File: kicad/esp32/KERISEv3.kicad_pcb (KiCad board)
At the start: 2 copper layers, 49 x 49 mm, 114 parts, among them P1 Motor_L, P10 PR_Host, P11 PR_Slave, P12 ENC_Host, P13 ENC_Slave, P14 ENC_Host, P15 ENC_Slave, P16 UART, P17 Fan, P18 PCB_ANT, P19 ANT_Host, P2 Motor_R, P3 Battery, P4 PR_Host, P5 PR_Slave, P6 PR_Host, P7 PR_Slave, P8 PR_Host, P9 PR_Slave, Q1 IRFML8244, Q2 IRFML8244, Q3 IRFML8244, Q4 IRFML8244, Q5 BSS138, Q6 IRFML8244, SW1 RESET, SW2 SW_PUSH_SMALL, U1 ESP32, U10 MPU6500, U11 AS5145, U12 AS5145, U2 XTAL, U3 FLASH, U4 DRV8835, U5 NJM2884, U6 AD8601, U7 AD8601, U8 AD8601, U9 AD8601

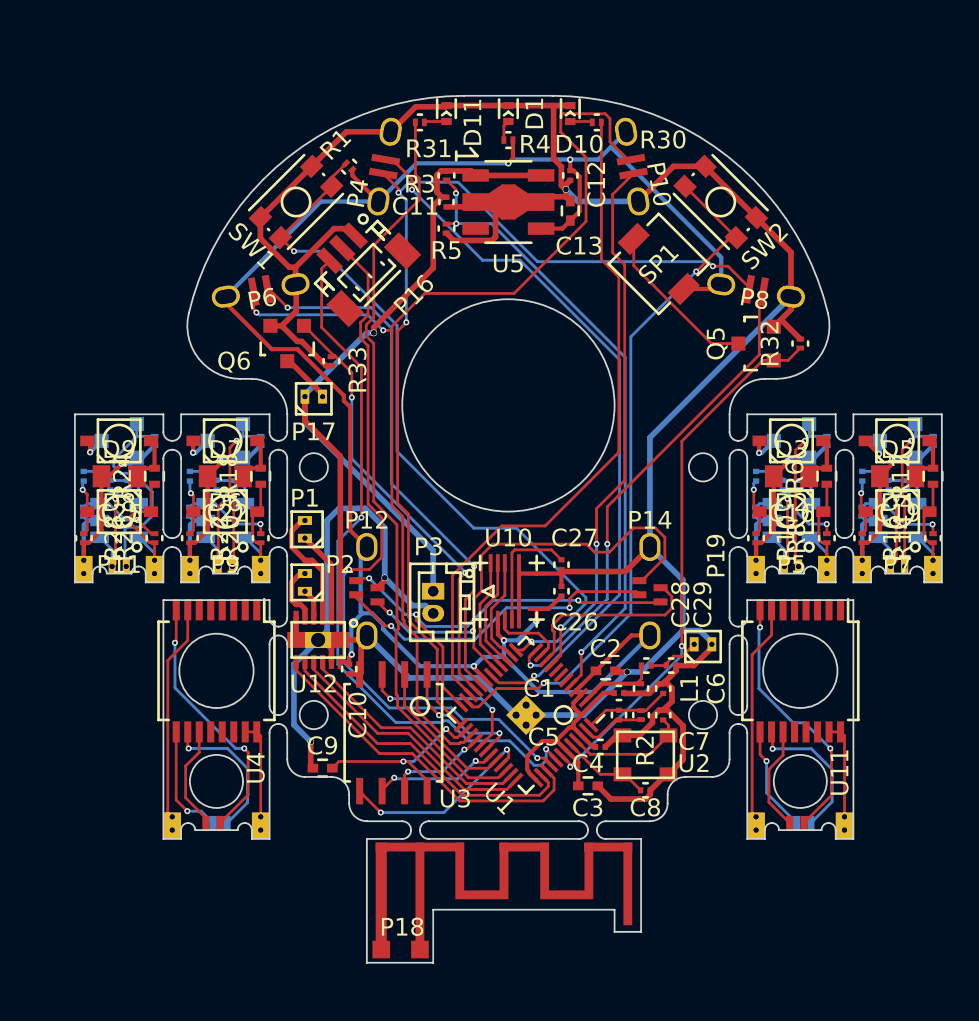
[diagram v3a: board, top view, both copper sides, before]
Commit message: 2輪の基板を作成
部品を配置
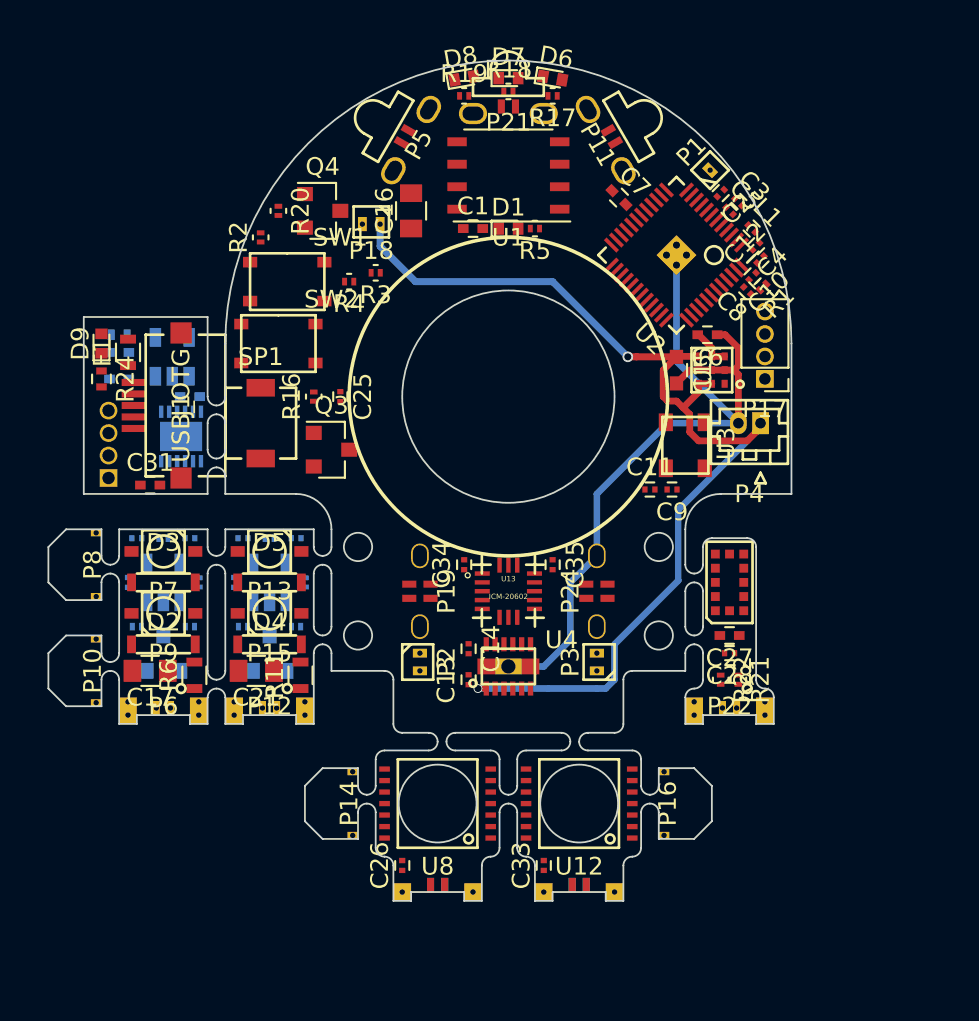
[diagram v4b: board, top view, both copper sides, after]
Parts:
- removed the C11 at (145.0, 91.0)
- removed the C12 at (152.0, 89.5)
- removed the C17 at (170.0, 107.0)
- removed the C18 at (168.5, 106.5)
- removed the C19 at (170.5, 106.5)
- removed the C21 at (130.5, 106.5)
- removed the C22 at (132.5, 106.5)
- removed the D4 at (170.5, 108.5)
- removed the D5 at (170.5, 104.5)
- removed the D6 at (132.5, 108.5)
- removed the D7 at (132.5, 104.5)
- removed the P12 at (140.5, 113.0)
- removed the P18 at (141.0, 132.8)
- removed the P6 at (134.5, 96.0)
- removed the Q2 at (170.5, 104.5)
- removed Q5: BSS138, TO_SOT_Packages_SMD:SOT-23
- removed the R12 at (172.5, 106.5)
- removed the R13 at (171.0, 107.0)
- removed the R14 at (172.5, 110.0)
- removed the R15 at (168.5, 108.5)
- removed the R17 at (172.5, 104.5)
- removed the R18 at (134.5, 106.5)
- removed the R20 at (134.5, 110.0)
- removed R29, R32: 10k, Resistors_SMD:R_0201
- removed the U3 at (142.0, 121.0)
- removed the U7 at (170.5, 109.0)
- added C15: 10u, Capacitors_SMD:C_0603, F.Cu at (158.0, 100.5)
- added C16: 47u, Capacitors_SMD:C_0805, F.Cu at (143.0, 91.5)
- added C2: 2.4p, Capacitors_SMD:C_0201, F.Cu at (160.5, 90.5)
- added C24: 0.1u, Capacitors_SMD:C_0201, B.Cu at (136.5, 110.0)
- added C25: 0.1u, Capacitors_SMD:C_0201, F.Cu at (139.0, 102.0)
- added C3: 3.9p, Capacitors_SMD:C_0201, F.Cu at (161.5, 91.0)
- added C30: 4.7u, Capacitors_SMD:C_0402, B.Cu at (126.5, 99.5)
- added C31: 0.1u, Capacitors_SMD:C_0402, F.Cu at (128.2, 107.0)
- added C32: 4.7u, Capacitors_SMD:C_0402, B.Cu at (126.5, 101.0)
- added C33: 0.1u, Capacitors_SMD:C_0201, F.Cu at (150.5, 128.5)
- added C34: 0.1u, Capacitors_SMD:C_0201, F.Cu at (146.0, 111.5)
- added C35: 0.1u, Capacitors_SMD:C_0201, F.Cu at (151.0, 111.5)
- added C4: 0.1u, Capacitors_SMD:C_0201, F.Cu at (162.5, 93.5)
- added D8: LED, LEDs:LED_0402, F.Cu at (146.0, 84.0)
- added D9: Status, LEDs:LED_0402, F.Cu at (125.5, 99.0)
- added F1: FEMTOSMDC035F-02, Resistors_SMD:R_0603, F.Cu at (127.0, 99.5)
- added J1: USB_OTG, mouse:ZX62R-B-5P, F.Cu at (130.0, 102.5)
- added P1: ANT, mouse:SMD_conn_1, F.Cu at (159.9, 89.2)
- added P10: Partition, mouse:Partition_Slave, F.Cu at (125.5, 117.5)
- added P17: COM, Pin_Headers:Pin_Header_Straight_1x04_Pitch1.27mm, F.Cu at (163.0, 101.0)
- added P20: ENC_Slave, mouse:STAND_AS_SLAVE, B.Cu at (144.5, 130.0)
- added P21: ToF_Host, mouse:STAND_PR_HOST, F.Cu at (148.5, 86.0)
- added P22: ToF_Slave, mouse:STAND_PR_SLAVE, F.Cu at (161.0, 120.0)
- added P23: COM, Socket_Strips:Socket_Strip_Straight_1x04_Pitch1.27mm, B.Cu at (125.9, 106.6)
- added P24: ENC_Host, mouse:STAND_AS_HOST, F.Cu at (153.5, 113.0)
- added P25: ENC_Slave, mouse:STAND_AS_SLAVE, B.Cu at (152.5, 130.0)
- added U1: FLASH, mouse:DFN-8-1EP_6x5mm_Pitch1.27mm_SmallFlag, F.Cu at (148.5, 89.5)
- added U13: ICM-20602, mouse:LGA-16-3x3, F.Cu at (148.5, 113.0)
- added U9: VL53L0X, mouse:VL53L0X, F.Cu at (161.0, 112.5)
- C13: value 4.7u -> 0.1u; footprint Capacitors_SMD:C_0402 -> Capacitors_SMD:C_0201
- C20: value 22p -> 0.1u
- C27: value 0.1u -> 4.7u; footprint Capacitors_SMD:C_0201 -> Capacitors_SMD:C_0402
- C28: value 4.7p -> 0.1u
- C29: value 2.4p -> 0.1u; footprint Capacitors_SMD:C_0201 -> Capacitors_SMD:C_0402; moved to B.Cu
- L1: value 2.4n -> 2.7n
- P13, P15: value ENC_Slave -> Partition; footprint mouse:STAND_AS_SLAVE -> mouse:Partition_Host; moved to F.Cu
- P14: value ENC_Host -> Partition; footprint mouse:STAND_AS_HOST -> mouse:Partition_Slave
- P16: value UART -> Partition; footprint Connectors_JST:JST_SH_BM03B-SRSS-TB_03x1.00mm_Straight -> mouse:Partition_Slave
- P19: value ANT_Host -> ENC_Host; footprint mouse:SMD_conn_2 -> mouse:STAND_AS_HOST
- P7, P9: value PR_Slave -> Partition; footprint mouse:STAND_PR_SLAVE -> mouse:Partition_Host
- P8: value PR_Host -> Partition; footprint mouse:STAND_PR_HOST -> mouse:Partition_Slave
- Q3: moved to F.Cu
- R11: value 10k -> 47; footprint Resistors_SMD:R_0201 -> Resistors_SMD:R_0603; moved to F.Cu
- R12: renamed from R28; moved to B.Cu
- R13: renamed from R26; moved to B.Cu
- R16: value 100k -> 1k
- R19: value 220k -> 1k; moved to F.Cu
- R21: value 1k -> 4.7k; moved to F.Cu
- R22: value 100k -> 4.7k
- R23: value 10k -> 4.7k; footprint Resistors_SMD:R_0201 -> Resistors_SMD:R_0402
- R24: value 100 -> 10k
- R6: value 100 -> 47; footprint Resistors_SMD:R_0402 -> Resistors_SMD:R_0603
- R7: renamed from R10; moved to B.Cu
- R8: moved to B.Cu
- SW1, SW2: footprint Buttons_Switches_SMD:SW_SPST_KMR2 -> mouse:SW_PUSH
- U10: value MPU6500 -> MCP73831; footprint mouse:MPU6500 -> TO_SOT_Packages_SMD:SOT-23-5; moved to B.Cu
- U11: value AS5145 -> FT234XD; footprint Housings_SSOP:SSOP-16_5.3x6.2mm_Pitch0.65mm -> Housings_DFN_QFN:DFN-12-1EP_3x3mm_Pitch0.45mm; moved to B.Cu
- U12: value AS5145 -> AS5048A; footprint Housings_SSOP:SSOP-16_5.3x6.2mm_Pitch0.65mm -> mouse:TSSOP-14_4.4x5mm_Pitch0.65mm
- U5: value NJM2884 -> LXDC2URxx; footprint TO_SOT_Packages_SMD:SOT89-5_Housing -> mouse:LXDC2UR
- U8: value AD8601 -> AS5048A; footprint TO_SOT_Packages_SMD:SOT-23-5 -> mouse:TSSOP-14_4.4x5mm_Pitch0.65mm; moved to F.Cu
- moved P7 41.5 mm to (129.0, 112.5), turned to 0 degrees
- moved P8 40.1 mm to (125.5, 111.5), turned to 90 degrees
- moved C17 37.9 mm to (128.2, 117.5)
- moved R6 37.5 mm to (130.8, 117.8)
- moved Q1 37.5 mm to (129.0, 116.5), turned to 90 degrees
- moved U11 37.4 mm to (130.0, 104.2)
- moved C19 37.4 mm to (127.0, 112.5)
- moved D2 36.8 mm to (129.0, 114.2)
- moved P6 36.4 mm to (129.0, 120.0)
- moved R8 36.3 mm to (130.5, 115.0), turned to 180 degrees
- moved U6 35.7 mm to (129.0, 112.5), turned to 90 degrees
- moved R9 35.6 mm to (127.5, 115.0), turned to 0 degrees
- moved D3 35.6 mm to (129.0, 110.8)
- moved C18 35.2 mm to (127.5, 110.0), turned to 180 degrees
- moved P16 34.9 mm to (157.0, 125.0), turned to 270 degrees
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- renumbered C9 to C1, C5 to C10, C8 to C11, C6 to C12, C10 to C14, C16 to C17, C15 to C18, C14 to C19, C25 to C21, C24 to C22, C1 to C5, C2 to C6, C3 to C7, C4 to C8, C7 to C9, D3 to D2, D2 to D3, D9 to D4, D8 to D5, D10 to D6, D11 to D7, P10 to P11, P11 to P12, P17 to P18, P1 to P2, P2 to P3, P3 to P4, P4 to P5, P5 to P6, Q4 to Q2, Q6 to Q4, R2 to R1, R7 to R10, R27 to R14, R25 to R15, R30 to R17, R31 to R18, R1 to R2, R33 to R20, R5 to R4, R4 to R5, U1 to U2, U2 to U3, U9 to U7
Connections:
- C13 pad 1: +3V3 -> +BATT
- C20 pad 1: /IR_RCV_FR/s_IR_RCV -> /IR_RCV_SL/s_3.3V
- C20 pad 2: Net-(C20-Pad2) -> /IR_RCV_SL/s_GND
- C26 pad 1: GND -> /Encoder_R/s_VDD
- C26 pad 2: +3V3 -> /Encoder_R/s_GND
- C27 pad 1: /AXIS_SENSOR/AXIS_CAP -> /ToF/s_3.3V
- C27 pad 2: GND -> /ToF/s_GND
- C28 pad 1: ANT -> /ToF/s_3.3V
- C28 pad 2: Net-(C28-Pad2) -> /ToF/s_GND
- C29 pad 1: Net-(C28-Pad2) -> /Writer/USB_5V
- C29 pad 2: GND -> /Writer/USB_GND
- L1 pad 1: ANT -> /ANTENA
- P11 pad 2: PR-LED-FL -> PR-LED-R
- P11 pad 3: PR-RCV-SR -> PR-RCV-R
- P13 pad 1: /ENC_L/s_3.3V -> (no net)
- P13 pad 2: /ENC_L/s_SCLK -> (no net)
- P14 pad 1: +3V3 -> (no net)
- P14 pad 2: ENC_SCK -> (no net)
- P15 pad 1: /ENC_R/s_3.3V -> (no net)
- P15 pad 2: /ENC_R/s_SCLK -> (no net)
- P16 pad 1: GND -> (no net)
- P16 pad 2: UART-RX -> (no net)
- P19 pad 1: Net-(C28-Pad2) -> +3V3
- P19 pad 2: GND -> SPI-CS-ENC
- P5 pad 2: PR-LED-FR -> PR-LED-L
- P5 pad 3: PR-RCV-SL -> PR-RCV-L
- P7 pad 1: /IR_RCV_FL/s_3.3V -> (no net)
- P7 pad 2: /IR_RCV_FL/s_IR_LED -> (no net)
- P8 pad 1: +3V3 -> (no net)
- P8 pad 2: PR-LED-FR -> (no net)
- P9 pad 1: /IR_RCV_FR/s_3.3V -> (no net)
- P9 pad 2: /IR_RCV_FR/s_IR_LED -> (no net)
- Q3 pad 1: /IR_RCV_FR/s_IR_LED -> SPEAKER
- Q3 pad 2: /IR_RCV_FR/s_GND -> GND
- Q3 pad 3: /IR_RCV_FR/LED_to_FET -> Net-(C25-Pad2)
- R11 pad 1: /IR_RCV_SL/s_IR_LED -> /IR_RCV_SR/s_3.3V
- R11 pad 2: /IR_RCV_SL/s_GND -> /IR_RCV_SR/LED_to_C
- R16 pad 1: Net-(C18-Pad2) (its old number) -> Net-(R16-Pad1)
- R16 pad 2: /IR_RCV_FL/s_GND -> Net-(C25-Pad1)
- R19 pad 1: /IR_RCV_FR/s_IR_RCV -> LED_3
- R19 pad 2: Net-(C20-Pad2) -> Net-(D8-Pad2)
- R21 pad 1: Net-(R20-Pad2) -> /ToF/s_3.3V
- R21 pad 2: /IR_RCV_FR/s_GND -> /ToF/s_SDA
- R22 pad 1: Net-(C21-Pad2) -> /ToF/s_3.3V
- R22 pad 2: /IR_RCV_FR/s_GND -> /ToF/s_SCL
- R23 pad 1: /IR_RCV_FR/s_IR_LED -> Net-(R23-Pad1)
- R23 pad 2: /IR_RCV_FR/s_GND -> /Writer/USB_GND
- R24 pad 1: /IR_RCV_SR/s_3.3V -> Net-(D9-Pad1)
- R24 pad 2: /IR_RCV_SR/LED_to_C -> Net-(R24-Pad2)
- SP1 pad 2: Net-(Q5-Pad3) -> Net-(R16-Pad1)
- U11 pad 1: (no net) -> /Writer/USB_D-
- U11 pad 10: /ENC_L/s_SCLK -> /Writer/USB_RX
- U11 pad 11: /ENC_L/s_CSn -> (no net)
- U11 pad 12: (no net) -> /Writer/USB_D+
- U11 pad 13: (no net) -> /Writer/USB_GND
- U11 pad 2: (no net) -> Net-(C31-Pad1)
- U11 pad 3: (no net) -> Net-(C31-Pad1)
- U11 pad 4: (no net) -> /Writer/USB_5V
- U11 pad 5: (no net) -> /Writer/USB_GND
- U11 pad 7: /ENC_L/s_VSS -> /Writer/USB_TX
- U11 pad 8: /ENC_L/s_MOSI -> (no net)
- U11 pad 9: /ENC_L/s_MISO -> Net-(C31-Pad1)
- U12 pad 1: (no net) -> /Encoder_L/s_CS
- U12 pad 10: /ENC_R/s_SCLK -> /Encoder_L/s_GND
- U12 pad 11: /ENC_R/s_CSn -> /Encoder_L/s_VDD
- U12 pad 12: (no net) -> /Encoder_L/s_VDD
- U12 pad 13: (no net) -> /Encoder_L/s_GND
- U12 pad 2: (no net) -> /Encoder_L/s_SCLK
- U12 pad 3: (no net) -> /Encoder_L/s_MISO
- U12 pad 4: (no net) -> /Encoder_L/s_MOSI
- U12 pad 5: (no net) -> /Encoder_L/s_GND
- U12 pad 6: (no net) -> /Encoder_L/s_GND
- U12 pad 7: /ENC_R/s_VSS -> /Encoder_L/s_GND
- U12 pad 8: /ENC_R/s_MOSI -> /Encoder_L/s_GND
- U12 pad 9: /ENC_R/s_MISO -> /Encoder_L/s_GND
- U2 pad 10: ENC_MISO -> PR-RCV-L
- U2 pad 11: AXIS_MISO -> (no net)
- U2 pad 12: PR-RCV-FR -> SPEAKER
- U2 pad 13: PR-RCV-SR -> FAN
- U2 pad 14: AXIS_~CS -> MT-IN-R1
- U2 pad 15: AXIS_SCK -> MT-IN-R2
- U2 pad 16: AXIS_MOSI -> PR-RCV-R
- U2 pad 17: ENC_~CS -> SPI-CS-AXIS
- U2 pad 18: PR-RCV-SL -> PR-LED-L
- U2 pad 2: ANT -> /ANTENA
- U2 pad 20: PR-RCV-FL -> PR-LED-R
- U2 pad 21: FAN -> SPI-CS-ENC
- U2 pad 24: ENC_SCK -> LED_2
- U2 pad 25: PR-LED-FR -> MT-IN-L1
- U2 pad 27: PR-LED-FL -> MT-IN-L2
- U2 pad 34: LED_2 -> LED_3
- U2 pad 35: MT-IN-L1 -> SPI-SCLK
- U2 pad 36: MT-IN-L2 -> SPI-MOSI
- U2 pad 38: MT-IN-R1 -> SPI-MISO
- U2 pad 39: MT-IN-R2 -> I2C-SCL
- U2 pad 42: SPEAKER -> I2C-SDA
- U5 pad 1: +BATT -> (no net)
- U5 pad 3: (no net) -> +3V3
- U8 pad 1: /IR_RCV_FR/s_IR_RCV -> /Encoder_R/s_CS
- U8 pad 2: /IR_RCV_FR/s_GND -> /Encoder_R/s_SCLK
- U8 pad 3: Net-(R20-Pad2) -> /Encoder_R/s_MISO
- U8 pad 4: Net-(C20-Pad2) -> /Encoder_R/s_MOSI
- U8 pad 5: /IR_RCV_FR/s_3.3V -> /Encoder_R/s_GND
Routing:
- net GND: track 195.9 -> 42.6 mm, vias 4 -> 0
- net +3V3: track 122.9 -> 2.31 mm, vias 6 -> 0
- net PR-LED-FL: track 61.5 -> 0.00 mm, vias 2 -> 0
- net PR-LED-FR: track 56.0 -> 0.00 mm, vias 3 -> 0
- net LED_2: track 43.2 -> 0.00 mm
- net PR-RCV-SL: track 41.0 -> 0.00 mm, vias 2 -> 0
- net UART-RX: track 40.4 -> 0.00 mm, vias 2 -> 0
- net UART-TX: track 40.3 -> 0.00 mm, vias 2 -> 0
- net Net-(R2-Pad1): track 40.3 -> 0.00 mm, vias 2 -> 0
- net BUTTON: track 39.6 -> 0.00 mm, vias 2 -> 0
- net LED_1: track 38.5 -> 0.00 mm
- net BAT-VOL: track 35.7 -> 0.00 mm, vias 3 -> 0
- net PR-RCV-SR: track 31.3 -> 0.00 mm, vias 2 -> 0
- net SPEAKER: track 30.8 -> 0.00 mm, vias 2 -> 0
- net PR-RCV-FL: track 30.6 -> 0.00 mm, vias 2 -> 0
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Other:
- board size 49 x 49 mm -> 42 x 47.5 mm
- net class 3.3V: clearance 0.16 -> 0.154; trace_width 0.238 -> 0.2; via_dia 0.36 -> 0.34
- net class BATT: clearance 0.16 -> 0.154; trace_width 0.32 -> 0.2; via_dia 0.38 -> 0.34; via_drill 0.32 -> 0.3
- net class Charger added: clearance 0.154, trace_width 0.24, via_dia 0.36, via_drill 0.3
- net class Default: clearance 0.16 -> 0.154; trace_width 0.16 -> 0.154; via_dia 0.34 -> 0.32
- net class GND: clearance 0.16 -> 0.154; trace_width 0.32 -> 0.24; via_dia 0.38 -> 0.36; via_drill 0.32 -> 0.3
- net class LED: clearance 0.16 -> 0.154; trace_width 0.24 -> 0.3
- net class Motor: clearance 0.16 -> 0.154; trace_width 0.3 -> 0.32; via_dia 0.36 -> 0.4; via_drill 0.3 -> 0.36
- rule trace_clearance: 0.16 -> 0.154
- rule trace_min: 0.16 -> 0.154
- rule via_min_size: 0.34 -> 0.32
